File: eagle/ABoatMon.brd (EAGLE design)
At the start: 87.6 x 61 mm, 33 parts, among them J1 VUSB, J2 GND, J3 GND, J4 LIPO, J5 U.FL, X1 MKDSN1,5/2-5,08

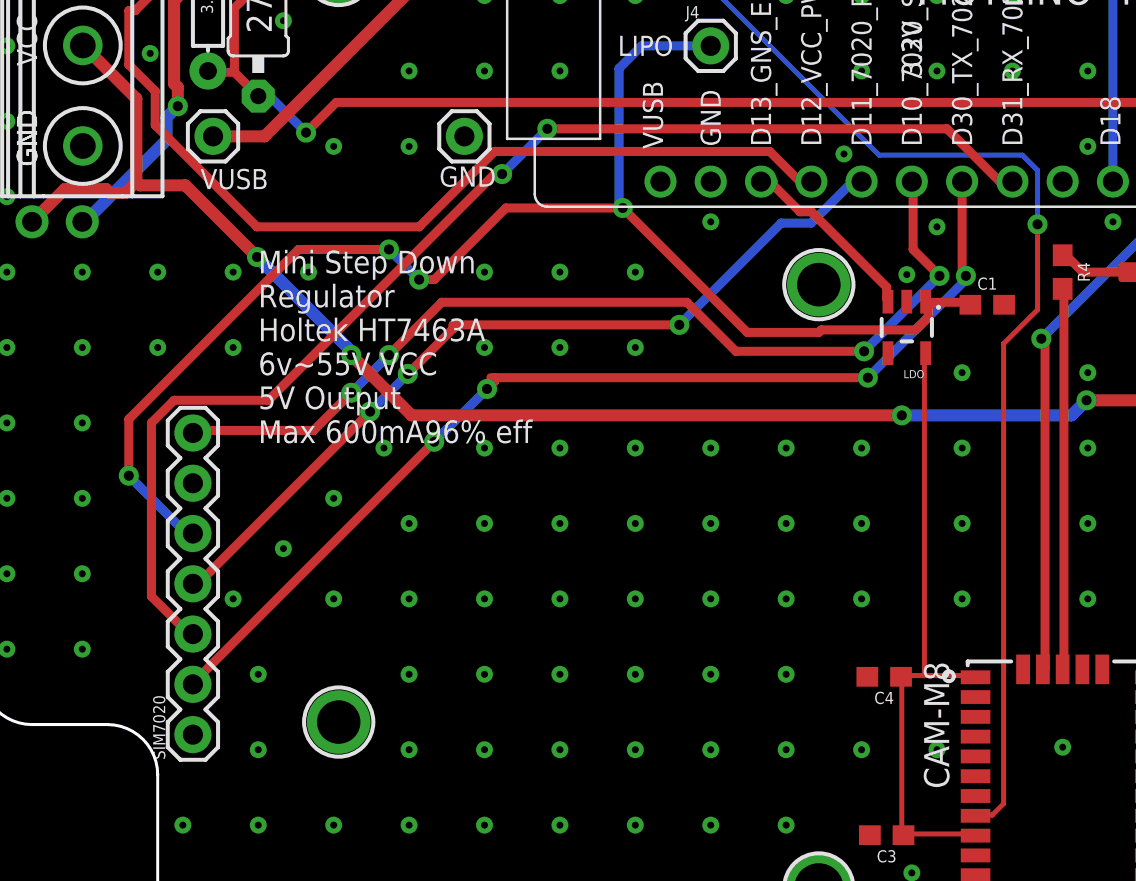
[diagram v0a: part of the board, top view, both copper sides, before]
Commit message: D7000 wrong way round, moved 10pin jst
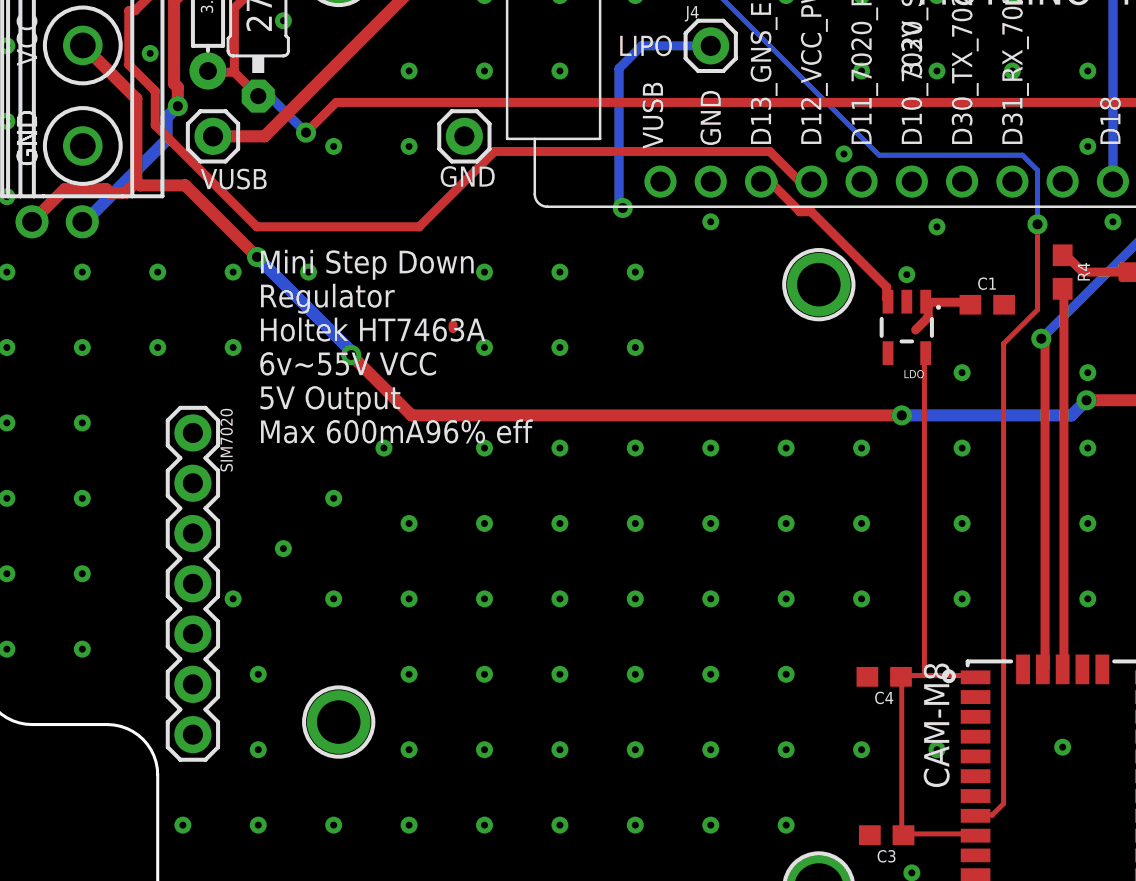
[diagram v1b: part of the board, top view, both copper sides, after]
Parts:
- moved SIM7020 15.2 mm to (10.7, 26.2), turned to 270 degrees
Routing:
- net D31_RX_7020: track 62.4 -> 0.00 mm, vias 2 -> 0
- net LIPO: track 71.9 -> 16.4 mm, vias 4 -> 1
- net D30_TX_7020: track 52.9 -> 0.00 mm, vias 4 -> 0
- net D10_7020_SLEEP: track 48.5 -> 0.00 mm, vias 4 -> 0
- net D11_7020_PWRKEY: track 43.1 -> 0.19 mm, vias 3 -> 0
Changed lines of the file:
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@@
 <attribute name="VALUE" x="58.801" y="33.655" size="0.6096" layer="27" font="vector" ratio="20" align="top-center"/>
 </element>
-<element name="SIM7020" library="SparkFun-Connectors" library_urn="urn:adsk.eagle:library:513" package="1X07" package3d_urn="urn:adsk.eagle:package:38129/1" value="SIMCOM" x="10.668" y="10.922" smashed="yes" rot="R90" grouprefs="SIMCOM">
-<attribute name="NAME" x="9.271" y="9.652" size="0.6096" layer="25" font="vector" ratio="20" rot="R90"/>
+<element name="SIM7020" library="SparkFun-Connectors" library_urn="urn:adsk.eagle:library:513" package="1X07" package3d_urn="urn:adsk.eagle:package:38129/1" value="SIMCOM" x="10.668" y="26.162" smashed="yes" rot="R270" grouprefs="SIMCOM">
+<attribute name="NAME" x="12.065" y="27.432" size="0.6096" layer="25" font="vector" ratio="20" rot="R270"/>
 </element>
 <element name="J4" library="SparkFun-Connectors" package="1X01" value="LIPO" x="36.83" y="45.72" smashed="yes">
@@
 <contactref element="U$6" pad="D30_TX"/>
 <contactref element="SIM7020" pad="2"/>
-<wire x1="49.53" y1="34.29" x2="49.53" y2="38.862" width="0.4572" layer="1"/>
-<wire x1="49.7205" y1="34.0995" x2="49.53" y2="34.29" width="0.4572" layer="1"/>
-<wire x1="49.7205" y1="33.909" x2="49.7205" y2="34.0995" width="0.4572" layer="16"/>
-<wire x1="44.7675" y1="28.956" x2="49.7205" y2="33.909" width="0.4572" layer="16"/>
-<wire x1="25.7175" y1="28.956" x2="25.908" y2="28.956" width="0.4572" layer="1"/>
-<via x="49.7205" y="34.0995" extent="1-16" drill="0.508"/>
-<via x="44.7675" y="28.956" extent="1-16" drill="0.508"/>
-<wire x1="25.908" y1="28.956" x2="44.7675" y2="28.956" width="0.4572" layer="1"/>
-<wire x1="22.86" y1="25.7175" x2="10.668" y2="13.5255" width="0.4572" layer="1"/>
-<wire x1="25.527" y1="28.3845" x2="22.86" y2="25.7175" width="0.4572" layer="16"/>
-<wire x1="25.908" y1="28.7655" x2="25.527" y2="28.3845" width="0.4572" layer="1"/>
-<wire x1="10.668" y1="13.5255" x2="10.668" y2="13.462" width="0.4572" layer="1"/>
-<wire x1="25.908" y1="28.7655" x2="25.908" y2="28.956" width="0.4572" layer="1"/>
-<via x="22.86" y="25.7175" extent="1-16" drill="0.508"/>
-<via x="25.527" y="28.3845" extent="1-16" drill="0.508"/>
+<wire x1="10.668" y1="23.622" x2="49.53" y2="38.862" width="0" layer="19" extent="1-1"/>
 </signal>
 <signal name="VCC" class="1">
@@
 <contactref element="U$6" pad="D31_RX"/>
 <contactref element="SIM7020" pad="3"/>
-<wire x1="48.768" y1="41.529" x2="51.435" y2="38.862" width="0.4572" layer="1"/>
-<wire x1="28.575" y1="41.529" x2="48.768" y2="41.529" width="0.4572" layer="1"/>
-<wire x1="26.289" y1="39.243" x2="28.575" y2="41.529" width="0.4572" layer="16"/>
-<wire x1="25.908" y1="39.243" x2="26.289" y2="39.243" width="0.4572" layer="1"/>
-<wire x1="14.478" y1="27.813" x2="25.908" y2="39.243" width="0.4572" layer="1"/>
-<wire x1="9.7155" y1="27.813" x2="14.478" y2="27.813" width="0.4572" layer="1"/>
-<wire x1="8.5725" y1="26.67" x2="9.7155" y2="27.813" width="0.4572" layer="1"/>
-<wire x1="8.5725" y1="17.907" x2="8.5725" y2="26.67" width="0.4572" layer="1"/>
-<wire x1="10.4775" y1="16.002" x2="8.5725" y2="17.907" width="0.4572" layer="1"/>
-<wire x1="10.4775" y1="16.002" x2="10.668" y2="16.002" width="0.4572" layer="1"/>
-<via x="28.575" y="41.529" extent="1-16" drill="0.508"/>
-<via x="26.289" y="39.243" extent="1-16" drill="0.508"/>
-<wire x1="51.435" y1="38.862" x2="52.07" y2="38.862" width="0.4572" layer="1"/>
+<wire x1="10.668" y1="21.082" x2="52.07" y2="38.862" width="0" layer="19" extent="1-1"/>
 </signal>
 <signal name="A1_VCC_VD">
@@
 <contactref element="U$6" pad="D10"/>
 <contactref element="SIM7020" pad="7"/>
-<wire x1="47.0535" y1="35.433" x2="47.0535" y2="38.862" width="0.4572" layer="1"/>
-<wire x1="48.387" y1="34.0995" x2="47.0535" y2="35.433" width="0.4572" layer="1"/>
-<wire x1="44.577" y1="30.2895" x2="48.387" y2="34.0995" width="0.4572" layer="16"/>
-<wire x1="38.1" y1="30.2895" x2="44.577" y2="30.2895" width="0.4572" layer="1"/>
-<wire x1="35.6235" y1="32.766" x2="38.1" y2="30.2895" width="0.4572" layer="1"/>
-<wire x1="23.241" y1="32.766" x2="35.6235" y2="32.766" width="0.4572" layer="1"/>
-<wire x1="47.0535" y1="38.862" x2="46.99" y2="38.862" width="0.4572" layer="1"/>
-<via x="48.387" y="34.0995" extent="1-16" drill="0.508"/>
-<via x="44.577" y="30.2895" extent="1-16" drill="0.508"/>
-<wire x1="16.764" y1="26.289" x2="10.668" y2="26.289" width="0.4572" layer="1"/>
-<wire x1="18.669" y1="28.194" x2="16.764" y2="26.289" width="0.4572" layer="1"/>
-<wire x1="20.574" y1="30.099" x2="18.669" y2="28.194" width="0.4572" layer="16"/>
-<wire x1="23.241" y1="32.766" x2="20.574" y2="30.099" width="0.4572" layer="1"/>
-<wire x1="10.668" y1="26.289" x2="10.668" y2="26.162" width="0.4572" layer="1"/>
-<via x="18.669" y="28.194" extent="1-16" drill="0.508"/>
-<via x="20.574" y="30.099" extent="1-16" drill="0.508"/>
+<wire x1="10.668" y1="10.922" x2="46.99" y2="38.862" width="0" layer="19" extent="1-1"/>
 </signal>
 <signal name="D11_7020_PWRKEY">
 <contactref element="U$6" pad="D11"/>
 <contactref element="SIM7020" pad="4"/>
-<wire x1="44.577" y1="38.2905" x2="44.577" y2="38.862" width="0.4572" layer="1"/>
-<wire x1="44.577" y1="38.862" x2="44.45" y2="38.862" width="0.4572" layer="1"/>
-<wire x1="44.0055" y1="38.862" x2="44.45" y2="38.862" width="0.4572" layer="16"/>
-<wire x1="41.91" y1="36.7665" x2="44.0055" y2="38.862" width="0.4572" layer="16"/>
-<wire x1="40.386" y1="36.7665" x2="41.91" y2="36.7665" width="0.4572" layer="16"/>
-<wire x1="35.2425" y1="31.623" x2="40.386" y2="36.7665" width="0.4572" layer="16"/>
-<wire x1="23.8125" y1="31.623" x2="35.2425" y2="31.623" width="0.4572" layer="1"/>
-<via x="35.2425" y="31.623" extent="1-16" drill="0.508"/>
-<wire x1="11.049" y1="18.669" x2="10.668" y2="18.669" width="0.4572" layer="1"/>
-<wire x1="19.6215" y1="27.2415" x2="11.049" y2="18.669" width="0.4572" layer="1"/>
-<wire x1="21.5265" y1="29.1465" x2="19.6215" y2="27.2415" width="0.4572" layer="16"/>
-<wire x1="23.8125" y1="31.4325" x2="21.5265" y2="29.1465" width="0.4572" layer="1"/>
-<wire x1="10.668" y1="18.669" x2="10.668" y2="18.542" width="0.4572" layer="1"/>
 <wire x1="23.8125" y1="31.4325" x2="23.8125" y2="31.623" width="0.4572" layer="1"/>
-<via x="19.6215" y="27.2415" extent="1-16" drill="0.508"/>
-<via x="21.5265" y="29.1465" extent="1-16" drill="0.508"/>
+<wire x1="23.8125" y1="31.623" x2="44.45" y2="38.862" width="0" layer="19" extent="1-1"/>
+<wire x1="10.668" y1="18.542" x2="23.8125" y2="31.4325" width="0" layer="19" extent="1-1"/>
 </signal>
 <signal name="N$2" class="2">
@@
 <wire x1="47.8155" y1="32.004" x2="47.8155" y2="32.5755" width="0.4572" layer="1"/>
 <wire x1="47.1805" y1="31.369" x2="47.8155" y2="32.004" width="0.4572" layer="1"/>
-<wire x1="42.418" y1="31.369" x2="47.1805" y2="31.369" width="0.4572" layer="1"/>
-<wire x1="42.291" y1="31.242" x2="42.418" y2="31.369" width="0.4572" layer="1"/>
-<wire x1="38.6715" y1="31.242" x2="42.291" y2="31.242" width="0.4572" layer="1"/>
-<wire x1="32.385" y1="37.5285" x2="38.6715" y2="31.242" width="0.4572" layer="1"/>
 <wire x1="47.8155" y1="32.5755" x2="47.686" y2="32.7961" width="0.4572" layer="1"/>
-<wire x1="32.385" y1="37.5285" x2="26.4795" y2="37.5285" width="0.4572" layer="1"/>
-<wire x1="10.287" y1="21.1455" x2="10.668" y2="21.1455" width="0.4572" layer="16"/>
-<wire x1="7.4295" y1="24.003" x2="10.287" y2="21.1455" width="0.4572" layer="16"/>
-<wire x1="7.4295" y1="26.8605" x2="7.4295" y2="24.003" width="0.4572" layer="1"/>
-<wire x1="16.002" y1="35.433" x2="7.4295" y2="26.8605" width="0.4572" layer="1"/>
-<wire x1="20.574" y1="35.433" x2="16.002" y2="35.433" width="0.4572" layer="1"/>
-<wire x1="22.098" y1="33.909" x2="20.574" y2="35.433" width="0.4572" layer="16"/>
-<wire x1="22.86" y1="33.909" x2="22.098" y2="33.909" width="0.4572" layer="1"/>
-<wire x1="26.4795" y1="37.5285" x2="22.86" y2="33.909" width="0.4572" layer="1"/>
-<wire x1="10.668" y1="21.1455" x2="10.668" y2="21.082" width="0.4572" layer="16"/>
-<via x="7.4295" y="24.003" extent="1-16" drill="0.508"/>
-<via x="20.574" y="35.433" extent="1-16" drill="0.508"/>
-<via x="22.098" y="33.909" extent="1-16" drill="0.508"/>
+<wire x1="32.385" y1="37.5285" x2="47.686" y2="32.7961" width="0" layer="19" extent="1-1"/>
+<wire x1="10.668" y1="16.002" x2="32.385" y2="37.5285" width="0" layer="19" extent="1-1"/>
 </signal>
 <signal name="N$6" class="1">

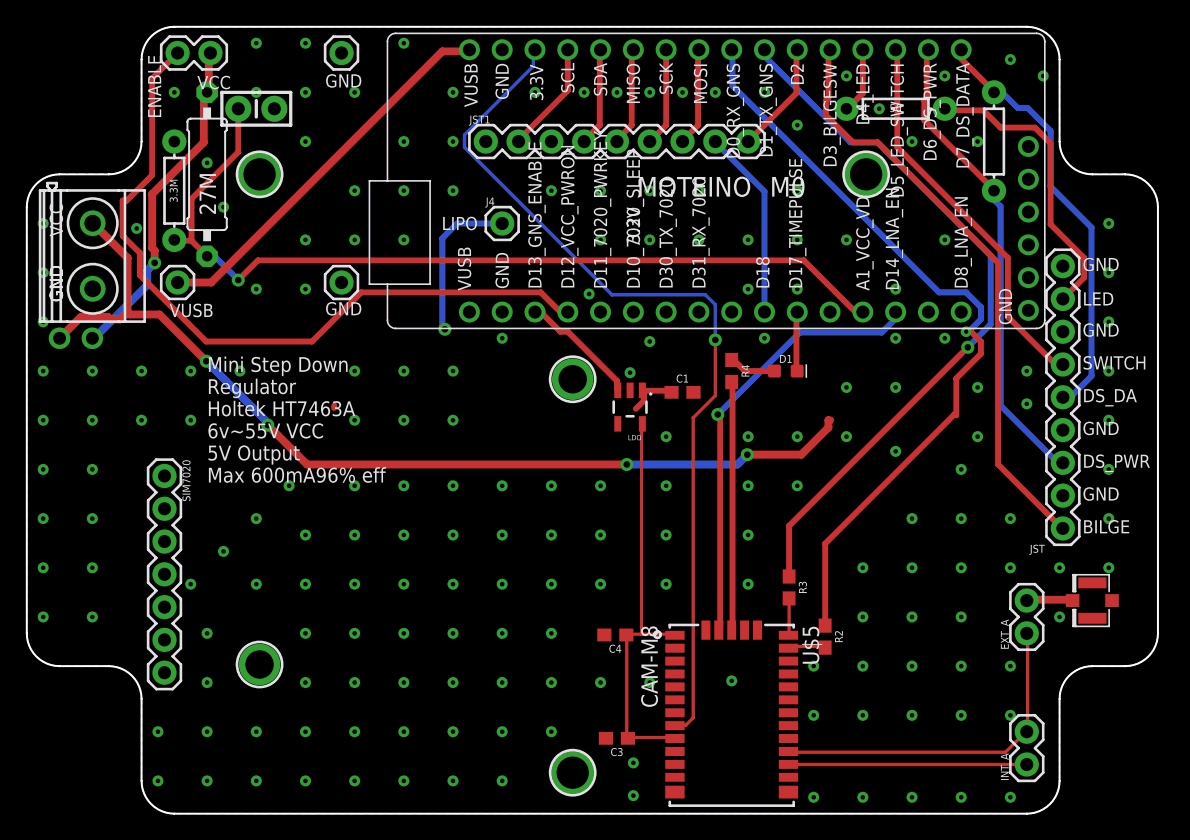
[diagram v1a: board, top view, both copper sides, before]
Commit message: Moved power jumper, added jumper txt
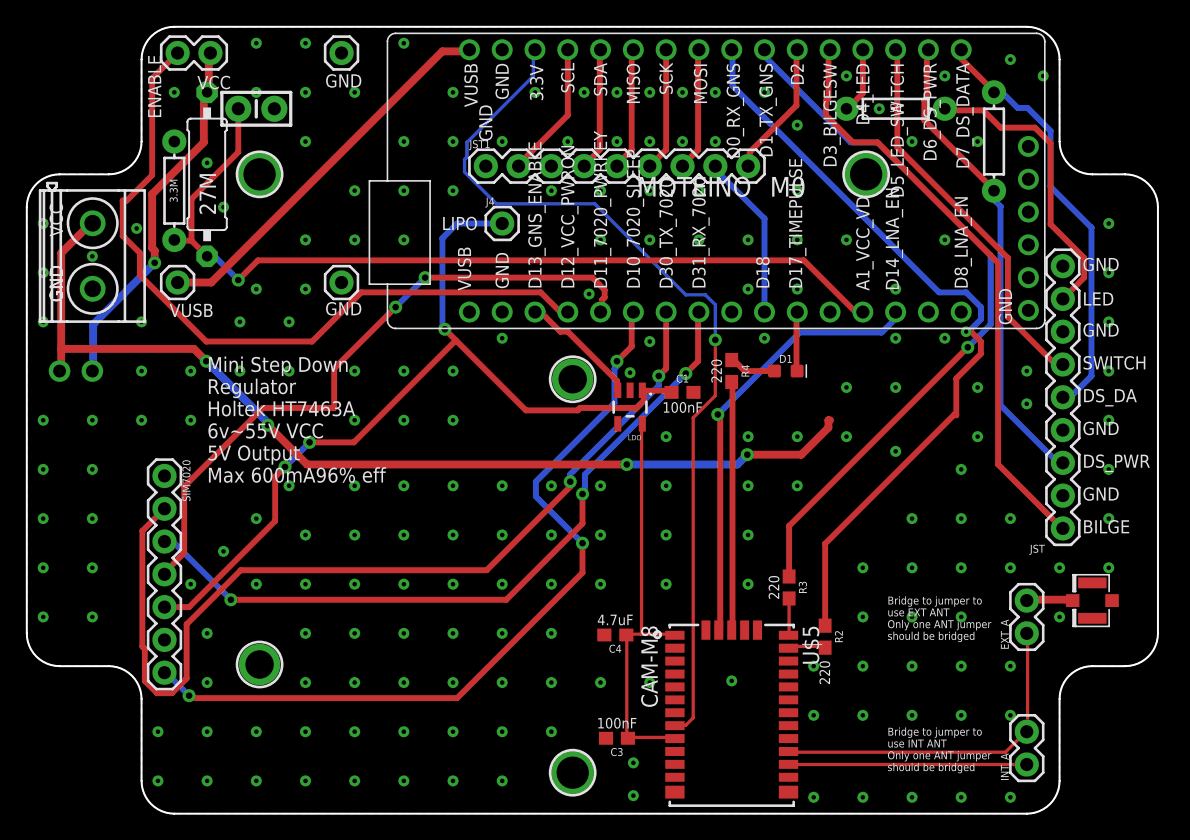
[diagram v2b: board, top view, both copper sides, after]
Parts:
- moved VCC 2.54 mm to (3.81, 34.3)
- moved JST1 1.91 mm to (35.6, 50.2)
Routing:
- net D30_TX_7020: track 0.00 -> 73.2 mm, vias 0 -> 2
- net D10_7020_SLEEP: track 0.00 -> 62.3 mm, vias 0 -> 3
- net D31_RX_7020: track 0.00 -> 56.9 mm, vias 0 -> 3
- net LIPO: track 16.4 -> 67.1 mm, vias 1 -> 3
- net D11_7020_PWRKEY: track 0.19 -> 50.8 mm, vias 0 -> 2
- net VCC_JUMPER: track 26.3 -> 28.7 mm
- net VCC: track 75.5 -> 77.8 mm
- net SCL: track 8.69 -> 10.6 mm
- net SCK: track 7.64 -> 9.54 mm
- net MISO: track 7.64 -> 9.54 mm
- net D2: track 8.68 -> 10.6 mm
- net SDA: track 7.62 -> 9.52 mm
- net MOSI: track 7.62 -> 9.52 mm
- net D18: track 14.8 -> 12.9 mm
- net 3.3V: track 68.7 -> 69.8 mm
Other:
- board text added: "Bridge to jumper to use EXT ANT Only one ANT jumper should be bridged"
- board text added: "Bridge to jumper to use INT ANT Only one ANT jumper should be bridged"

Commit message: Clearance DRC errors fixed
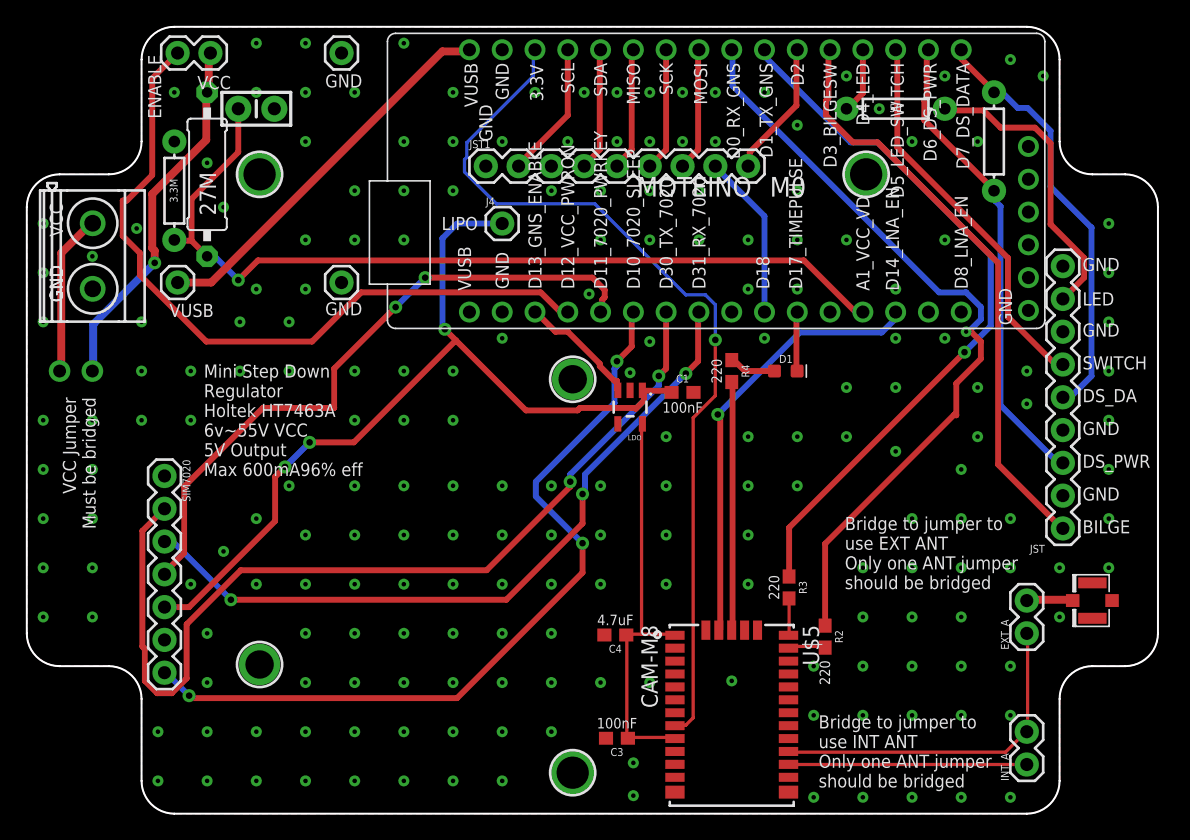
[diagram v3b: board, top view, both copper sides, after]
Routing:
- net VCC: track 77.8 -> 12.7 mm, vias 4 -> 0
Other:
- board text added: "VCC Jumper Must be bridged"

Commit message: DRC, ERC checked.  Moved routes away from GNS chip
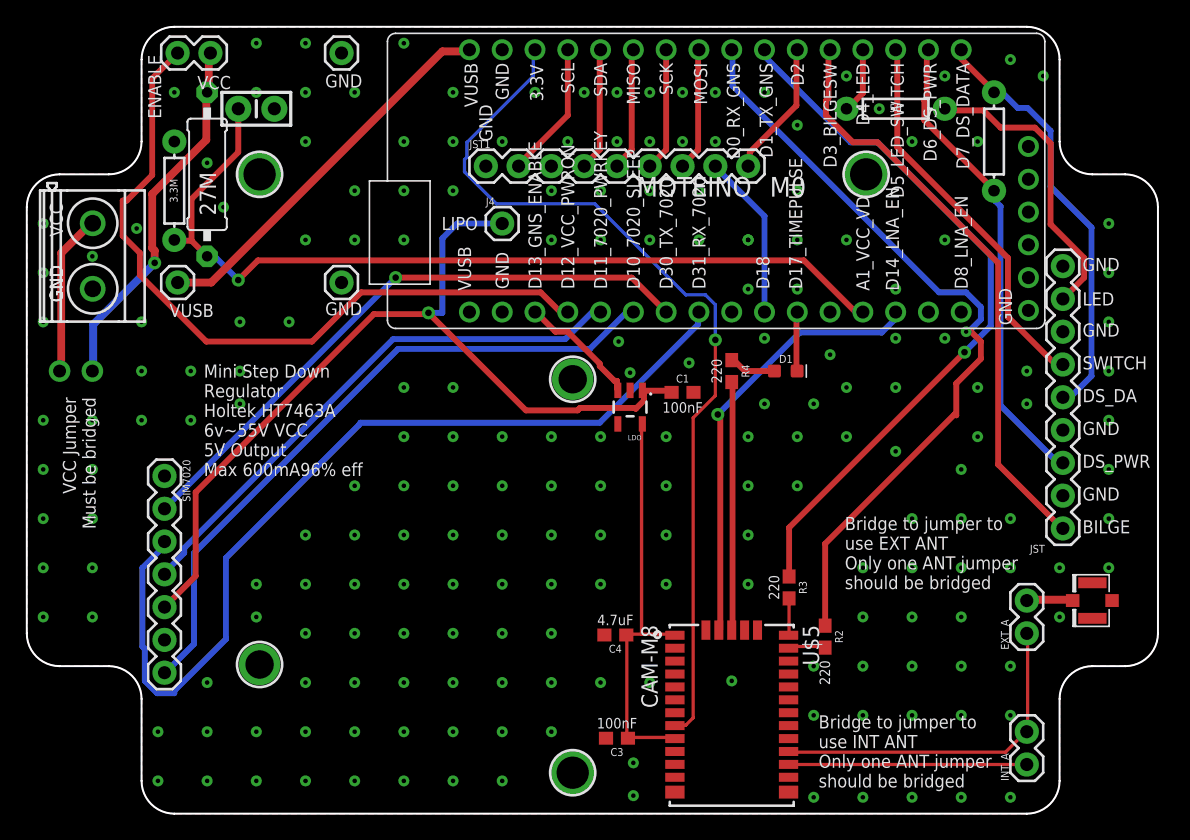
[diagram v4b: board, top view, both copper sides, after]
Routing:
- net D30_TX_7020: track 73.2 -> 47.4 mm, vias 2 -> 1
- net D31_RX_7020: track 56.9 -> 71.5 mm, vias 3 -> 0
- net D10_7020_SLEEP: track 62.3 -> 52.1 mm, vias 3 -> 0
- net D11_7020_PWRKEY: track 50.8 -> 42.5 mm, vias 2 -> 0
- net LIPO: track 67.1 -> 69.0 mm, vias 3 -> 1
